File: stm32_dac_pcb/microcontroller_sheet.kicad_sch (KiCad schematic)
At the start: 19 parts, among them J201 Conn_01x03, J202 Conn_01x05, J204 USB_C_Receptacle_USB2.0, SW201 SW_Push, SW202 SW_Push, SW203 SW_Push, U101 STM32F411CEUx

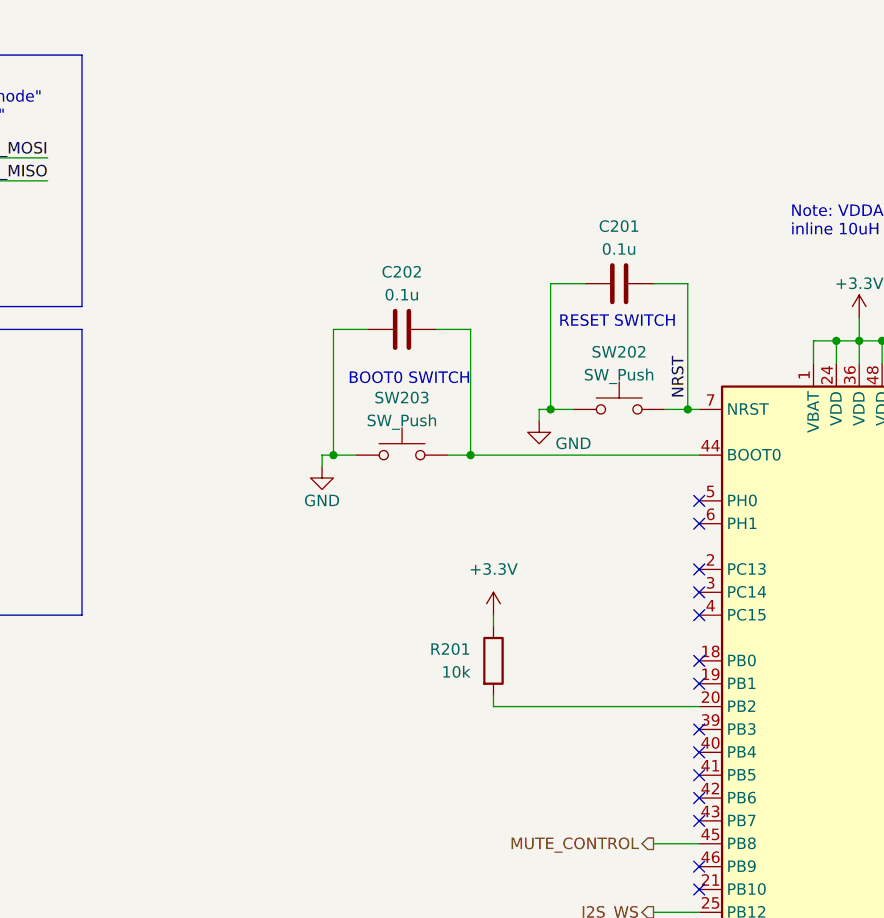
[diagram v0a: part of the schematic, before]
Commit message: Add FIXME notes for assembly, update LCSC numbers in BOM
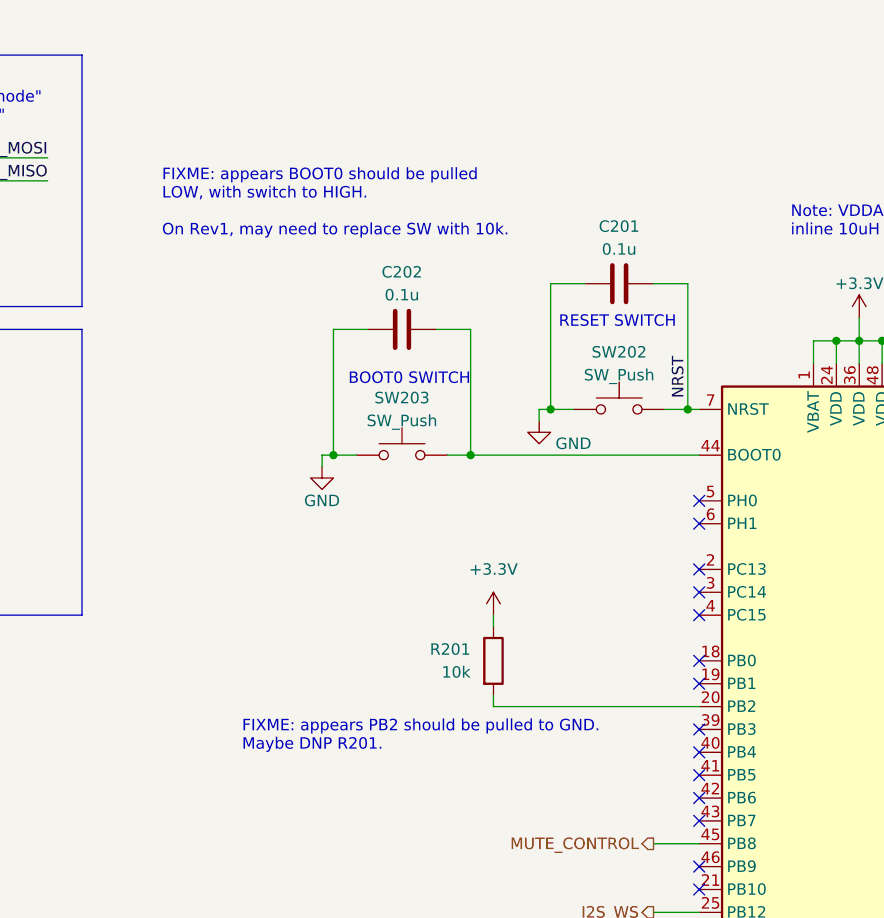
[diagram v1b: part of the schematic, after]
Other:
- note added: "FIXME: appears BOOT0 should be pulled LOW, with switch to HIGH. On Rev1, may need to replace SW with 10k."
- note added: "FIXME: appears PB2 should be pulled to GND. Maybe DNP R201."
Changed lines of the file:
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@@
     (effects (font (size 1.27 1.27)) (justify left bottom) (href "https://dubiouscreations.com/2021/04/06/designing-with-usb-c-lessons-learned/"))
+  )
+  (text "FIXME: appears BOOT0 should be pulled\nLOW, with switch to HIGH.\n\nOn Rev1, may need to replace SW with 10k."
+    (at 63.5 41.91 0)
+    (effects (font (size 1.27 1.27)) (justify left bottom))
   )
   (text "Chosen Connector:\n  LCSC C165948\n\n\nAlt Option:\n  USB: LCSC C2686966\n  G-Switch GT-USB-7029DB\n"
@@
     (effects (font (size 1.27 1.27)) (justify right bottom))
   )
+  (text "FIXME: appears PB2 should be pulled to GND.\nMaybe DNP R201."
+    (at 72.39 99.06 0)
+    (effects (font (size 1.27 1.27)) (justify left bottom))
+  )
   (text "Note: VDDA has an \ninline 10uH on Pill" (at 133.35 41.91 0)

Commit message: Bump to KiCAD v8
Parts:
- renumbered C307 to C203, C307 to C204, C307 to C205, C307 to C206, C307 to C207, U101 to U201

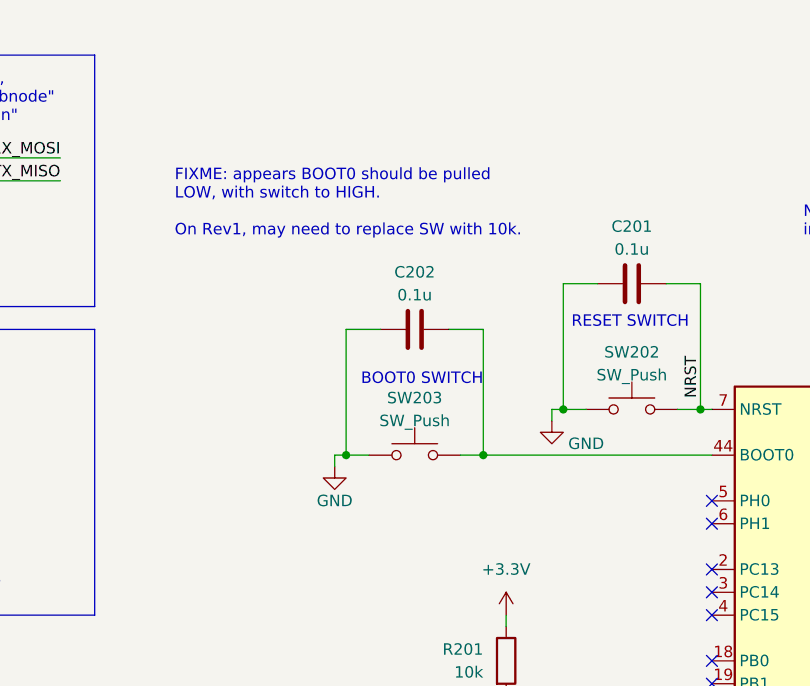
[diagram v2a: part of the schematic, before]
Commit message: Schematic: Add 100u cap, fix BOOT0
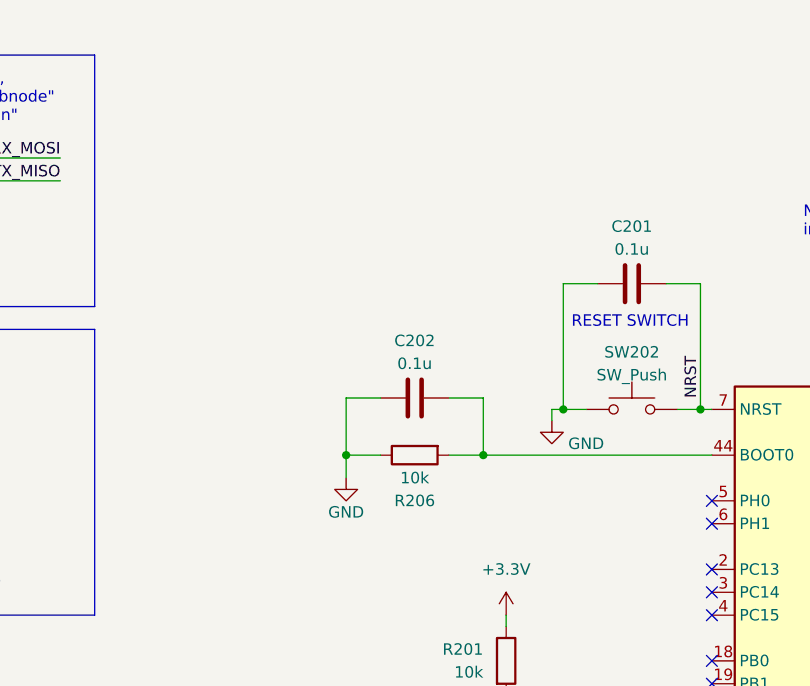
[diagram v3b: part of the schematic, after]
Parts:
- removed SW203: SW_Push, 0_project_fp_lib:PushButtonSMD_2.93x3.9, symbol Switch:SW_Push
- added R206: 10k, Resistor_SMD:R_0603_1608Metric_Pad0.98x0.95mm_HandSolder, symbol Device:R
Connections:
- net GND: now also R206.1
- net at C202.2, U201.44 (BOOT0): now also R206.2
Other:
- note removed: "BOOT0 SWITCH"
- note removed: "FIXME: appears BOOT0 should be pulled LOW, with switch to HIGH. On Rev1, may need to replace SW with 10k."
- moved on the sheet: C202
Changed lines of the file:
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@@
 	(wire
 		(pts
-			(xy 86.36 52.07) (xy 82.55 52.07)
+			(xy 86.36 59.69) (xy 82.55 59.69)
 		)
 		(stroke
@@
 	(wire
 		(pts
-			(xy 81.28 67.31) (xy 81.28 66.04)
+			(xy 82.55 68.58) (xy 82.55 66.04)
 		)
 		(stroke
@@
 	(wire
 		(pts
-			(xy 82.55 52.07) (xy 82.55 66.04)
+			(xy 82.55 59.69) (xy 82.55 66.04)
 		)
 		(stroke
@@
 	(wire
 		(pts
-			(xy 93.98 52.07) (xy 97.79 52.07)
+			(xy 93.98 59.69) (xy 97.79 59.69)
 		)
 		(stroke
@@
 	(wire
 		(pts
-			(xy 95.25 66.04) (xy 97.79 66.04)
+			(xy 93.98 66.04) (xy 97.79 66.04)
 		)
 		(stroke
@@
 	(wire
 		(pts
-			(xy 97.79 52.07) (xy 97.79 66.04)
+			(xy 97.79 59.69) (xy 97.79 66.04)
 		)
 		(stroke
@@
 	(wire
 		(pts
-			(xy 82.55 66.04) (xy 85.09 66.04)
+			(xy 82.55 66.04) (xy 86.36 66.04)
 		)
 		(stroke
@@
 	(wire
 		(pts
-			(xy 81.28 66.04) (xy 82.55 66.04)
-		)
-		(stroke
-			(width 0)
-			(type default)
-		)
-	)
-	(wire
-		(pts
 			(xy 228.6 33.02) (xy 242.57 33.02)
 		)
@@
 		)
 	)
-	(text "FIXME: appears BOOT0 should be pulled\nLOW, with switch to HIGH.\n\nOn Rev1, may need to replace SW with 10k."
-		(exclude_from_sim no)
-		(at 63.5 41.91 0)
-		(effects
-			(font
-				(size 1.27 1.27)
-			)
-			(justify left bottom)
-		)
-	)
 	(text "Chosen Connector:\n  LCSC C165948\n\n\nAlt Option:\n  USB: LCSC C2686966\n  G-Switch GT-USB-7029DB\n"
 		(exclude_from_sim no)
@@
 		)
 	)
-	(text "BOOT0 SWITCH"
-		(exclude_from_sim no)
-		(at 97.79 58.42 0)
-		(effects
-			(font
-				(size 1.27 1.27)
-			)
-			(justify right bottom)
-		)
-	)
 	(label "USB_DN"
 		(at 58.42 152.4 180)
@@
 	(symbol
 		(lib_id "Device:R")
+		(at 90.17 66.04 90)
+		(mirror x)
+		(unit 1)
+		(exclude_from_sim no)
+		(in_bom yes)
+		(on_board yes)
+		(dnp no)
+		(property "Reference" "R206"
+			(at 90.17 71.12 90)
+			(effects
+				(font
+					(size 1.27 1.27)
+				)
+			)
+		)
+		(property "Value" "10k"
+			(at 90.17 68.58 90)
+			(effects
+				(font
+					(size 1.27 1.27)
+				)
+			)
+		)
+		(property "Footprint" "Resistor_SMD:R_0603_1608Metric_Pad0.98x0.95mm_HandSolder"
+			(at 90.17 64.262 90)
+			(effects
+				(font
+					(size 1.27 1.27)
+				)
+				(hide yes)
+			)
+		)
+		(property "Datasheet" "~"
+			(at 90.17 66.04 0)
+			(effects
+				(font
+					(size 1.27 1.27)
+				)
+				(hide yes)
+			)
+		)
+		(property "Description" ""
+			(at 90.17 66.04 0)
+			(effects
+				(font
+					(size 1.27 1.27)
+				)
+				(hide yes)
+			)
+		)
+		(pin "1"
+		)
+		(pin "2"
+		)
+		(instances
+			(project "stm32_dac_pcb"
+				(path "/c2a919d7-4260-41a9-9bc5-9737c1b4d769/b77d31d3-d267-4ae4-806f-e210a5dd1f2c"
+					(reference "R206")
+					(unit 1)
+				)
+			)
+		)
+	)
+	(symbol
+		(lib_id "Device:R")
 		(at 67.31 153.67 0)
 		(mirror y)
@@
 	(symbol
 		(lib_id "Device:C")
-		(at 90.17 52.07 90)
+		(at 90.17 59.69 90)
 		(unit 1)
 		(exclude_from_sim no)
@@
 		(dnp no)
 		(property "Reference" "C202"
-			(at 90.17 45.72 90)
+			(at 90.17 53.34 90)
 			(effects
 				(font
@@
 		)
 		(property "Value" "0.1u"
-			(at 90.17 48.26 90)
+			(at 90.17 55.88 90)
 			(effects
 				(font
@@
 		)
 		(property "Footprint" "Capacitor_SMD:C_0603_1608Metric_Pad1.08x0.95mm_HandSolder"
-			(at 93.98 51.1048 0)
+			(at 93.98 58.7248 0)
 			(effects
 				(font
@@
 		)
 		(property "Datasheet" "~"
-			(at 90.17 52.07 0)
+			(at 90.17 59.69 0)
 			(effects
 				(font
@@
 		)
 		(property "Description" ""
-			(at 90.17 52.07 0)
+			(at 90.17 59.69 0)
 			(effects
 				(font
@@
 	(symbol
 		(lib_id "Switch:SW_Push")
-		(at 90.17 66.04 0)
-		(mirror y)
-		(unit 1)
-		(exclude_from_sim no)
-		(in_bom yes)
-		(on_board yes)
-		(dnp no)
-		(property "Reference" "SW203"
-			(at 90.17 59.69 0)
-			(effects
-				(font
-					(size 1.27 1.27)
-				)
-			)
-		)
-		(property "Value" "SW_Push"
-			(at 90.17 62.23 0)
-			(effects
-				(font
-					(size 1.27 1.27)
-				)
-			)
-		)
-		(property "Footprint" "0_project_fp_lib:PushButtonSMD_2.93x3.9"
-			(at 90.17 60.96 0)
-			(effects
-				(font
-					(size 1.27 1.27)
-				)
-				(hide yes)
-			)
-		)
-		(property "Datasheet" "~"
-			(at 90.17 60.96 0)
-			(effects
-				(font
-					(size 1.27 1.27)
-				)
-				(hide yes)
-			)
-		)
-		(property "Description" ""
-			(at 90.17 66.04 0)
-			(effects
-				(font
-					(size 1.27 1.27)
-				)
-				(hide yes)
-			)
-		)
-		(property "LCSC" "C18077675"
-			(at 90.17 66.04 0)
-			(effects
-				(font
-					(size 1.27 1.27)
-				)
-				(hide yes)
-			)
-		)
-		(pin "2"
-		)
-		(pin "1"
-		)
-		(instances
-			(project "stm32_dac_pcb"
-				(path "/c2a919d7-4260-41a9-9bc5-9737c1b4d769/b77d31d3-d267-4ae4-806f-e210a5dd1f2c"
-					(reference "SW203")
-					(unit 1)
-				)
-			)
-		)
-	)
-	(symbol
-		(lib_id "Switch:SW_Push")
 		(at 114.3 60.96 0)
 		(mirror y)
@@
 	(symbol
 		(lib_id "power:GND")
-		(at 81.28 67.31 0)
+		(at 82.55 68.58 0)
 		(mirror y)
 		(unit 1)
@@
 		(dnp no)
 		(property "Reference" "#PWR0205"
-			(at 81.28 73.66 0)
+			(at 82.55 74.93 0)
 			(effects
 				(font
@@
 		)
 		(property "Value" "GND"
-			(at 81.28 71.12 0)
+			(at 82.55 72.39 0)
 			(effects
 				(font
@@
 		)
 		(property "Footprint" ""
-			(at 81.28 67.31 0)
+			(at 82.55 68.58 0)
 			(effects
 				(font
@@
 		)
 		(property "Datasheet" ""
-			(at 81.28 67.31 0)
+			(at 82.55 68.58 0)
 			(effects
 				(font
@@
 		)
 		(property "Description" ""
-			(at 81.28 67.31 0)
+			(at 82.55 68.58 0)
 			(effects
 				(font

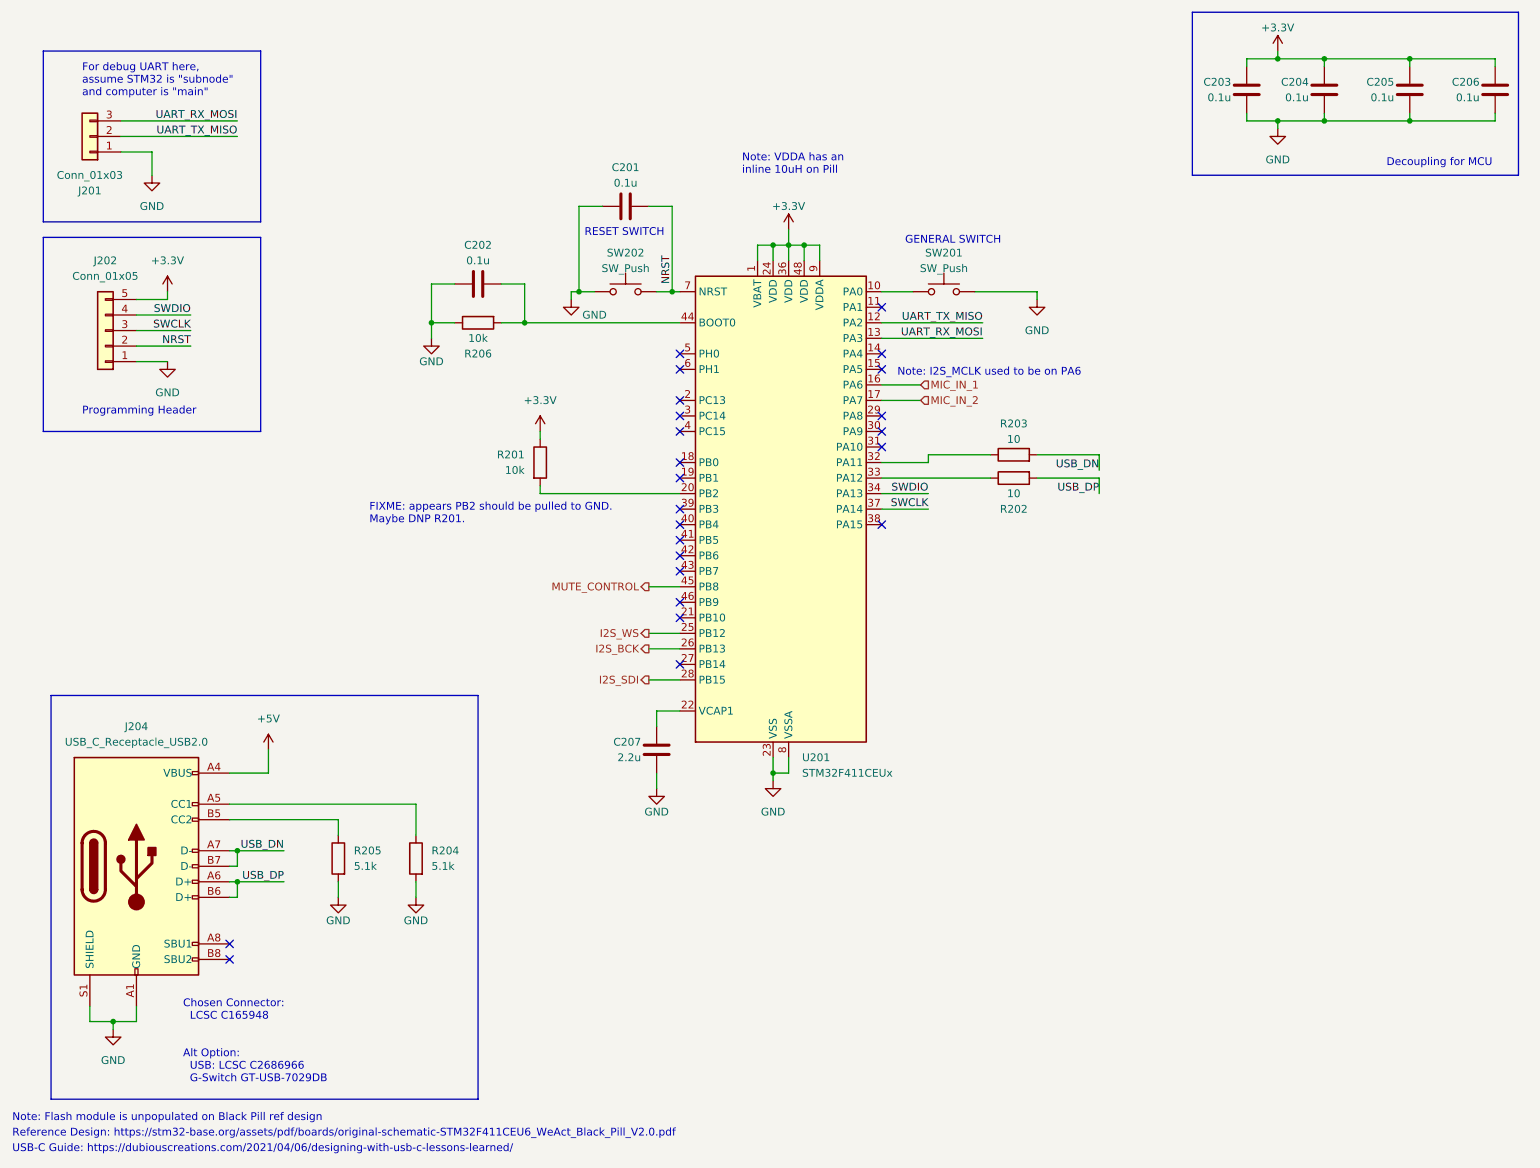
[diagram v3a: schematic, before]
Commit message: Finish layout with crystal
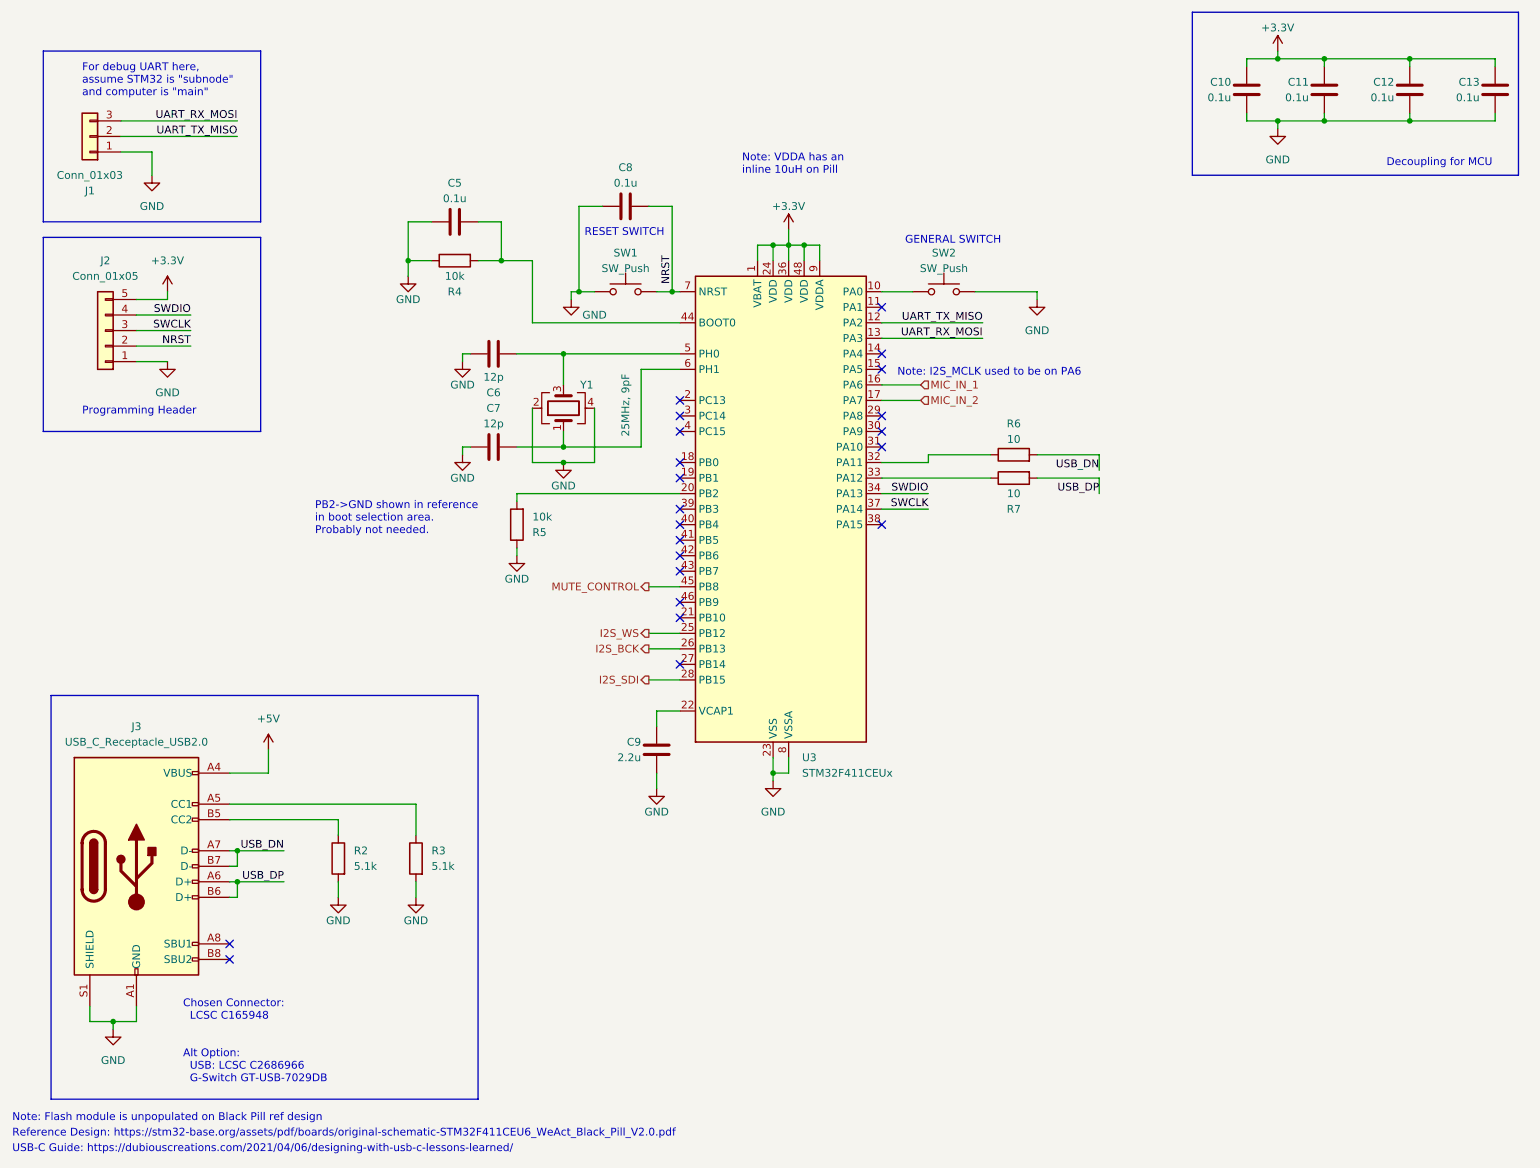
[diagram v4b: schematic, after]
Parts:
- added C6, C7: 12p, Capacitor_SMD:C_0603_1608Metric_Pad1.08x0.95mm_HandSolder, symbol Device:C
- added Y1: 25MHz, 9pF, Crystal:Crystal_SMD_2520-4Pin_2.5x2.0mm, symbol Device:Crystal_GND24
- renumbered C203 to C10, C204 to C11, C205 to C12, C206 to C13, C202 to C5, C201 to C8, C207 to C9, J201 to J1, J202 to J2, J204 to J3, R205 to R2, R204 to R3, R206 to R4, R201 to R5, R203 to R6, R202 to R7, SW202 to SW1, SW201 to SW2, U201 to U3
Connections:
- net +3.3V: no longer R5.1
- net GND: now also R5.1, C6.1, C7.1, Y1.2, Y1.4
- net at U3.5 (PH0): now also C6.2, Y1.3
- net at U3.6 (PH1): now also C7.2, Y1.1
- no-connect marks 24 -> 22
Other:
- note added: "PB2->GND shown in reference in boot selection area. Probably not needed."
- note removed: "FIXME: appears PB2 should be pulled to GND. Maybe DNP R201."
- moved on the sheet: C5, R4, R5
